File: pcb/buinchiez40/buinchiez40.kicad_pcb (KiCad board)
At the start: 2 copper layers, 120 x 40 mm, 89 parts, among them SW1 SW_Push, SW10 SW_Push, SW11 SW_Push, SW12 SW_Push, SW13 SW_Push, SW14 SW_Push, SW15 SW_Push, SW16 SW_Push, SW17 SW_Push, SW18 SW_Push, SW19 SW_Push, SW2 SW_Push, SW20 SW_Push, SW21 SW_Push, SW22 SW_Push, SW23 SW_Push, SW24 SW_Push, SW25 SW_Push, SW26 SW_Push, SW27 SW_Push, SW28 SW_Push, SW29 SW_Push, SW3 SW_Push, SW30 SW_Push, SW31 SW_Push, SW32 SW_Push, SW33 SW_Push, SW34 SW_Push, SW35 SW_Push, SW36 SW_Push, SW37 SW_Push, SW38 SW_Push, SW39 SW_Push, SW4 SW_Push, SW40 SW_Push, SW5 SW_Push, SW6 SW_Push, SW7 SW_Push, SW8 SW_Push, SW9 SW_Push

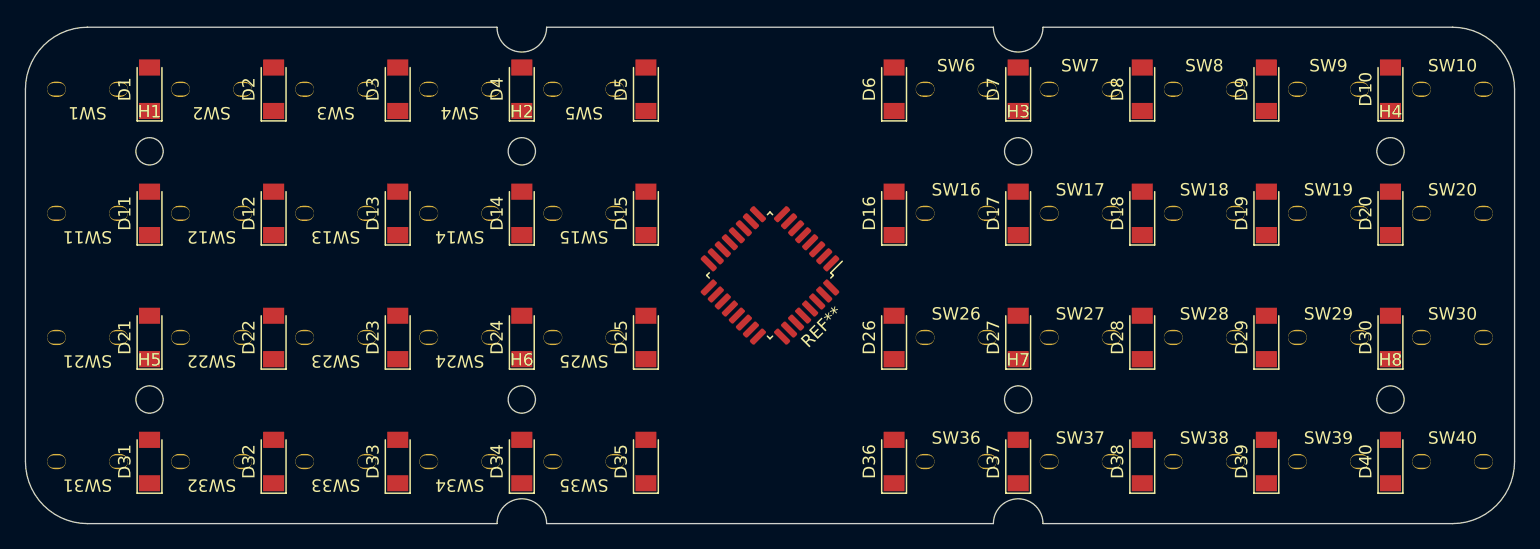
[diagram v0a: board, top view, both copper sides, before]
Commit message: add pcb output and cases
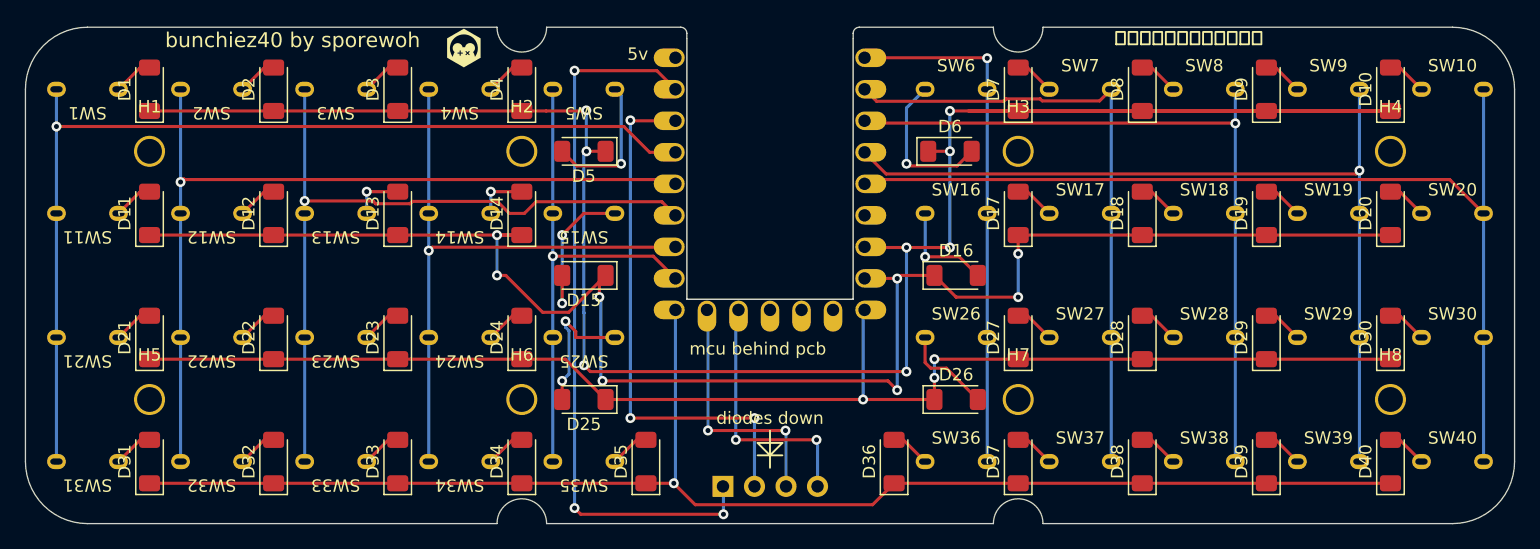
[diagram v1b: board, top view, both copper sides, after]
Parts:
- removed REF**: LQFP-32_7x7mm_P0.8mm, Package_QFP:LQFP-32_7x7mm_P0.8mm
- added J1: OLED-128x32, display:OLED-128x32-cutout, B.Cu at (151.0, 93.6)
- added U1: rp2040-zero, mcu:rp2040-zero-tht, F.Cu at (145.0, 67.6)
- H1, H2, H3, H4, H5, H6, H7, H8: footprint MountingHole:MountingHole_2.2mm_M2 -> userlib:m1.6_hole
- moved D15 7.07 mm to (130.0, 75.0), turned to 180 degrees
- moved D16 7.07 mm to (160.0, 75.0), turned to 0 degrees
- moved D25 7.07 mm to (130.0, 85.0), turned to 180 degrees
- moved D26 7.07 mm to (160.0, 85.0), turned to 0 degrees
- moved D5 7.07 mm to (130.0, 65.0), turned to 180 degrees
- moved D6 6.73 mm to (159.5, 65.0), turned to 0 degrees
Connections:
- net Net-(D1-Pad1) renamed row1
- net Net-(D11-Pad1) renamed row2
- net Net-(D21-Pad1) renamed row3
- net Net-(D31-Pad1) renamed row4
- net Net-(SW1-Pad2) renamed col1
- net Net-(SW10-Pad2) renamed col10
- net Net-(SW12-Pad2) renamed col2
- net Net-(SW13-Pad2) renamed col3
- net Net-(SW14-Pad2) renamed col4
- net Net-(SW15-Pad2) renamed col5
- net Net-(SW16-Pad2) renamed col6
- net Net-(SW17-Pad2) renamed col7
- net Net-(SW18-Pad2) renamed col8
- net Net-(SW19-Pad2) renamed col9
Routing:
- net row1: track 0.00 -> 182.7 mm, vias 0 -> 8
- net row2: track 0.00 -> 136.5 mm, vias 0 -> 8
- net row4: track 0.00 -> 115.8 mm, vias 0 -> 1
- net row3: track 0.00 -> 111.9 mm, vias 0 -> 3
- net col10: track 0.00 -> 81.2 mm
- net col1: track 0.00 -> 80.7 mm, vias 0 -> 1
- net col2: track 0.00 -> 71.1 mm, vias 0 -> 1
- net col9: track 0.00 -> 70.7 mm, vias 0 -> 1
- net col3: track 0.00 -> 61.3 mm, vias 0 -> 1
- net col8: track 0.00 -> 60.0 mm, vias 0 -> 1
- net gnd: track 0.00 -> 58.5 mm, vias 0 -> 3
- net col7: track 0.00 -> 50.8 mm
- net col4: track 0.00 -> 50.0 mm, vias 0 -> 1
- net 3v3: track 0.00 -> 43.1 mm, vias 0 -> 3
- net col6: track 0.00 -> 42.4 mm, vias 0 -> 1
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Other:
- outline, holes or cut-outs redrawn
- board text added: "5v"
- board text added: "bunchiez40 by sporewoh"
- board text added: "diodes down"
- board text added: "mcu behind pcb"
- board text added: "とても小さい、とても嫌な"

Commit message: add grounding pads
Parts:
- H1, H2, H3, H4, H5, H6, H7, H8: value MountingHole -> MountingHole_Pad
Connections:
- H1 pad 1: (no net) -> gnd
- H2 pad 1: (no net) -> gnd
- H3 pad 1: (no net) -> gnd
- H4 pad 1: (no net) -> gnd
- H5 pad 1: (no net) -> gnd
- H6 pad 1: (no net) -> gnd
- H7 pad 1: (no net) -> gnd
- H8 pad 1: (no net) -> gnd
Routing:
- net gnd: track 58.5 -> 312.5 mm, vias 3 -> 5
